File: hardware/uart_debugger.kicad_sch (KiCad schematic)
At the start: 3 parts, among them Q3 JSM2302, U3 CH340E UART Module

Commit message: Added switch footprint, SparkFun_LiPower footprint
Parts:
- U3: now left out of the parts list
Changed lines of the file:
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@@
 		(unit 1)
 		(exclude_from_sim no)
-		(in_bom yes)
+		(in_bom no)
 		(on_board yes)
 		(dnp no)

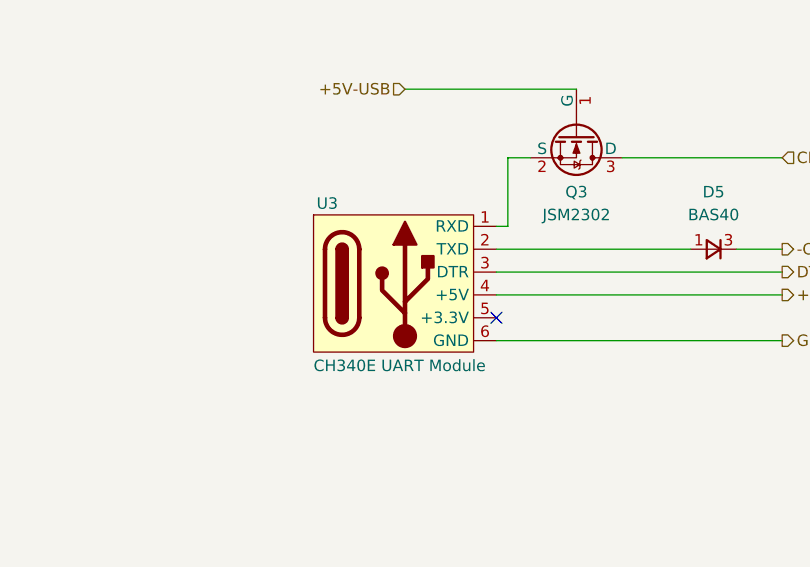
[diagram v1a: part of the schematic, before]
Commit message: Added many footprints and populated part of the property tables
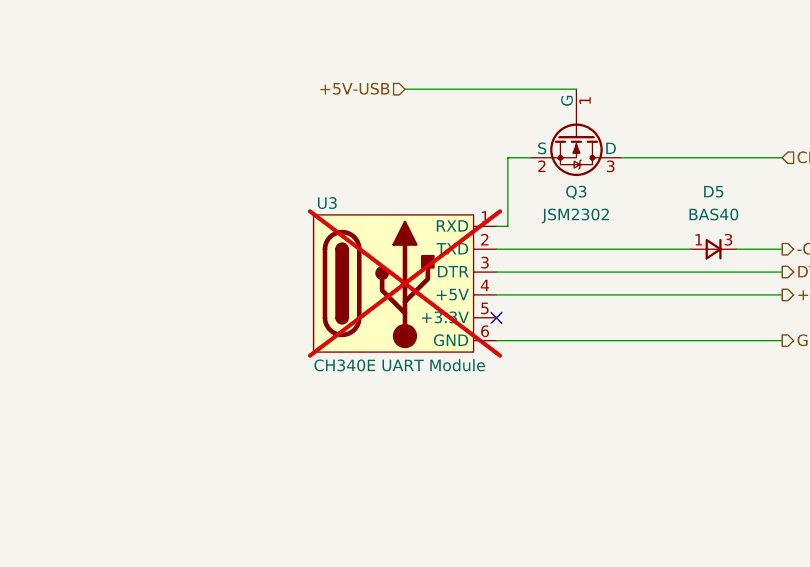
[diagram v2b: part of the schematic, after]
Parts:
- U3: now not fitted
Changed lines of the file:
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@@
 		(in_bom no)
 		(on_board yes)
-		(dnp no)
+		(dnp yes)
 		(property "Reference" "U3"
 			(at 117.094 95.25 0)

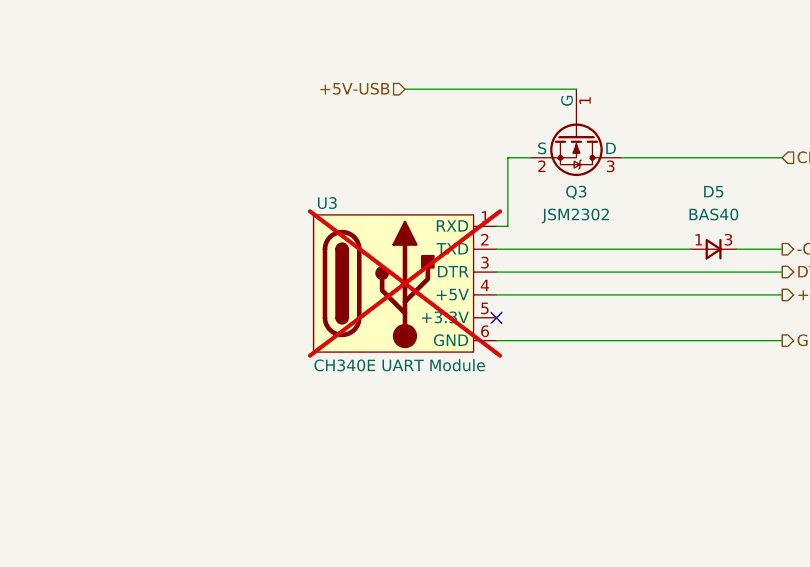
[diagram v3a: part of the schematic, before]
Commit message: Made some small changes on the properties of some components while having last weeks meeting and added the fp-info-cache to the gitignore file
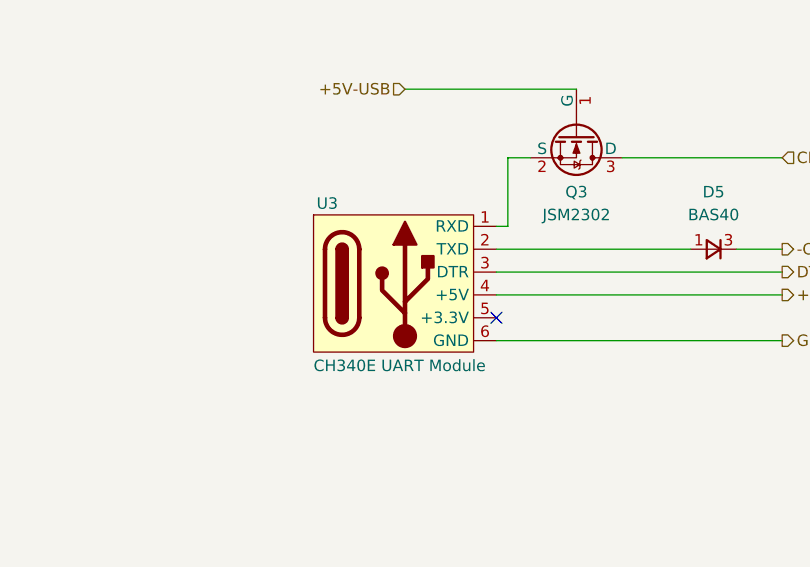
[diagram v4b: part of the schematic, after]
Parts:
- U3: now fitted
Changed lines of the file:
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@@
 		(in_bom no)
 		(on_board yes)
-		(dnp yes)
+		(dnp no)
 		(property "Reference" "U3"
 			(at 117.094 95.25 0)

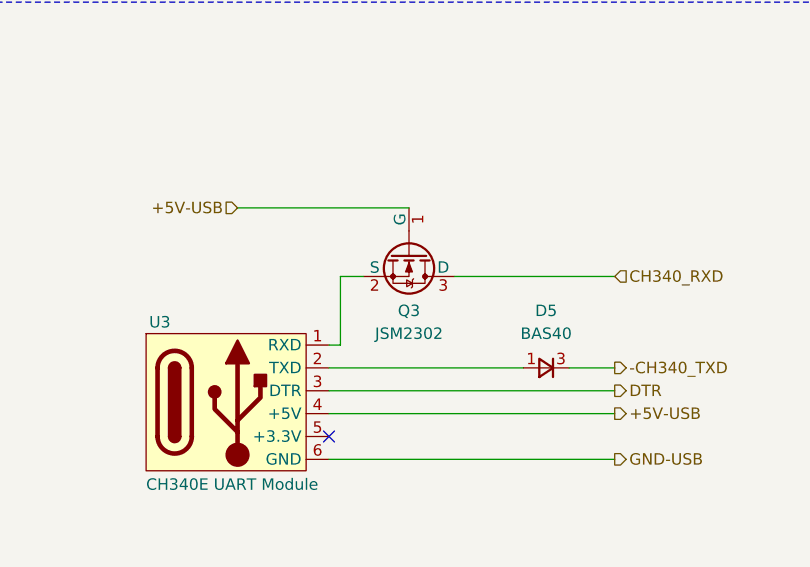
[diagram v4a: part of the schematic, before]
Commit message: Symbols pins vs footprint pins checked
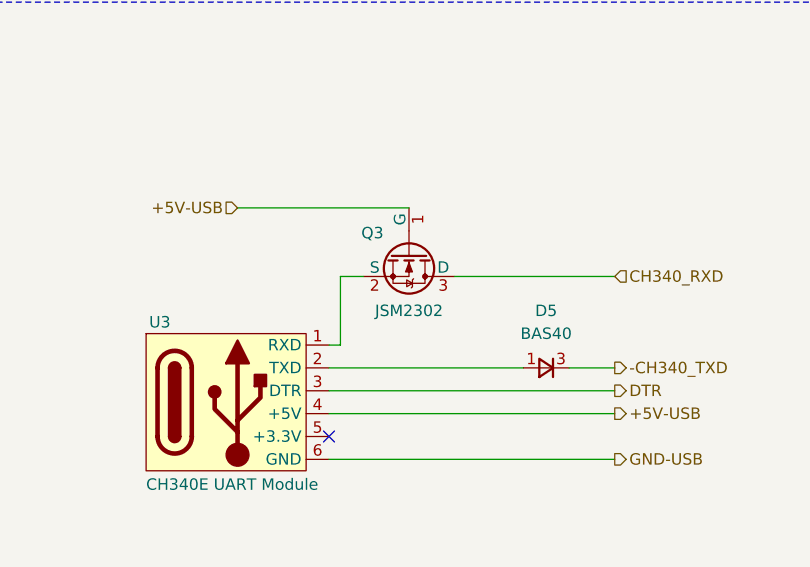
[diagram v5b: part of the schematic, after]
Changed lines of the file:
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@@
 		(dnp no)
 		(property "Reference" "Q3"
-			(at 144.78 93.98 90)
+			(at 140.716 85.344 90)
 			(effects
 				(font
@@
 		)
 		(property "Value" "JSM2302"
-			(at 144.78 96.52 90)
+			(at 144.78 93.98 90)
 			(effects
 				(font

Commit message: Electric Rules Check completed.
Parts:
- removed D5: BAS40, Package_TO_SOT_SMD:SOT-23, symbol Device:D_Small
- removed Q3: JSM2302, Package_TO_SOT_SMD:SOT-23, symbol Simulation_SPICE:NMOS
- added D2: BAS40, Package_TO_SOT_SMD:SOT-23, symbol kitchen_timer-symbols_lib:BAS40_diode
- added Q4: JSM2302, Package_TO_SOT_SMD:SOT-23, symbol kitchen_timer-symbols_lib:JSM2302
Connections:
- net +5V-USB: now also Q4.1 (G)
- net CH340_RXD: now also Q4.3 (D)
- net ­CH340_TXD: now also D2.3 (K)
- net at U3.1 (RXD): now also Q4.2 (S)
- net at U3.2 (TXD): now also D2.1 (A)
- net GND-USB renamed GND
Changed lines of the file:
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@@
 	)
 	(hierarchical_label "+5V-USB"
-		(shape input)
+		(shape output)
 		(at 125.73 82.55 180)
 		(effects
@@
 		)
 	)
-	(hierarchical_label "GND-USB"
+	(hierarchical_label "GND"
 		(shape output)
 		(at 167.64 110.49 0)
@@
 	)
 	(symbol
-		(lib_id "Simulation_SPICE:NMOS")
+		(lib_id "kitchen_timer-symbols_lib:BAS40_diode")
+		(at 160.02 100.33 180)
+		(unit 1)
+		(exclude_from_sim no)
+		(in_bom yes)
+		(on_board yes)
+		(dnp no)
+		(fields_autoplaced yes)
+		(property "Reference" "D2"
+			(at 160.02 93.98 0)
+			(effects
+				(font
+					(size 1.27 1.27)
+				)
+			)
+		)
+		(property "Value" "BAS40"
+			(at 160.02 96.52 0)
+			(effects
+				(font
+					(size 1.27 1.27)
+				)
+			)
+		)
+		(property "Footprint" "Package_TO_SOT_SMD:SOT-23"
+			(at 138.938 100.076 90)
+			(effects
+				(font
+					(size 1.27 1.27)
+				)
+				(hide yes)
+			)
+		)
+		(property "Datasheet" "https://jlcpcb.com/api/file/downloadByFileSystemAccessId/8590224761860497408"
+			(at 142.748 101.092 90)
+			(effects
+				(font
+					(size 1.27 1.27)
+				)
+				(hide yes)
+			)
+		)
+		(property "Description" "40V Independent Type 200mA 1V@40mA SOT-23 Schottky Diodes ROHS"
+			(at 158.75 118.872 0)
+			(effects
+				(font
+					(size 1.27 1.27)
+				)
+				(hide yes)
+			)
+		)
+		(property "Sim.Pins" "1=K 2=A"
+			(at 148.844 110.998 0)
+			(effects
+				(font
+					(size 1.27 1.27)
+				)
+				(hide yes)
+			)
+		)
+		(property "Supplier Link" "https://jlcpcb.com/partdetail/78417-BAS40/C77289"
+			(at 156.21 121.412 0)
+			(effects
+				(font
+					(size 1.27 1.27)
+				)
+				(hide yes)
+			)
+		)
+		(property "Package" "SOT-23"
+			(at 158.496 115.316 0)
+			(effects
+				(font
+					(size 1.27 1.27)
+				)
+				(hide yes)
+			)
+		)
+		(property "Supplier Name" "JLCPCB"
+			(at 160.02 100.33 0)
+			(effects
+				(font
+					(size 1.27 1.27)
+				)
+				(hide yes)
+			)
+		)
+		(property "Manuf. Part #" "BAS40"
+			(at 160.02 100.33 0)
+			(effects
+				(font
+					(size 1.27 1.27)
+				)
+				(hide yes)
+			)
+		)
+		(property "Supplier Unit Price" "$0.0257"
+			(at 160.02 100.33 0)
+			(effects
+				(font
+					(size 1.27 1.27)
+				)
+				(hide yes)
+			)
+		)
+		(property "Part Num" "NA"
+			(at 160.02 100.33 0)
+			(effects
+				(font
+					(size 1.27 1.27)
+				)
+				(hide yes)
+			)
+		)
+		(property "Manuf. Name" "Jiangsu Changjing Electronics Technology Co., Ltd."
+			(at 160.02 100.33 0)
+			(effects
+				(font
+					(size 1.27 1.27)
+				)
+				(hide yes)
+			)
+		)
+		(property "Supplier Part #" " C77289"
+			(at 160.02 100.33 0)
+			(effects
+				(font
+					(size 1.27 1.27)
+				)
+				(hide yes)
+			)
+		)
+		(pin "3"
+		)
+		(pin "1"
+		)
+		(instances
+			(project ""
+				(path "/8963deea-96bc-4401-b671-98fbe9ed9c6a/f7e640d9-c0d9-4c44-8592-f18e152ed7d5"
+					(reference "D2")
+					(unit 1)
+				)
+			)
+		)
+	)
+	(symbol
+		(lib_id "kitchen_timer-symbols_lib:JSM2302")
 		(at 144.78 87.63 270)
 		(unit 1)
@@
 		(on_board yes)
 		(dnp no)
-		(property "Reference" "Q3"
-			(at 140.716 85.344 90)
+		(property "Reference" "Q4"
+			(at 140.208 84.836 90)
 			(effects
 				(font
@@
 		)
 		(property "Value" "JSM2302"
-			(at 144.78 93.98 90)
+			(at 144.78 93.726 90)
 			(effects
 				(font
@@
 			)
 		)
-		(property "Sim.Type" "VDMOS"
+		(property "Sim.Type" ""
 			(at 125.73 87.63 0)
 			(effects
@@
 			)
 		)
-		(property "Sim.Pins" "1=D 2=G 3=S"
+		(property "Sim.Pins" ""
 			(at 129.54 87.63 0)
 			(effects
@@
 			(project ""
 				(path "/8963deea-96bc-4401-b671-98fbe9ed9c6a/f7e640d9-c0d9-4c44-8592-f18e152ed7d5"
-					(reference "Q3")
+					(reference "Q4")
 					(unit 1)
 				)
-			)
-		)
-	)
-	(symbol
-		(lib_name "D_Small_1")
-		(lib_id "Device:D_Small")
-		(at 160.02 100.33 0)
-		(mirror y)
-		(unit 1)
-		(exclude_from_sim no)
-		(in_bom yes)
-		(on_board yes)
-		(dnp no)
-		(property "Reference" "D5"
-			(at 160.02 93.98 0)
-			(effects
-				(font
-					(size 1.27 1.27)
-				)
-			)
-		)
-		(property "Value" "BAS40"
-			(at 160.02 96.52 0)
-			(effects
-				(font
-					(size 1.27 1.27)
-				)
-			)
-		)
-		(property "Footprint" "Package_TO_SOT_SMD:SOT-23"
-			(at 138.938 100.584 90)
-			(effects
-				(font
-					(size 1.27 1.27)
-				)
-				(hide yes)
-			)
-		)
-		(property "Datasheet" "https://jlcpcb.com/api/file/downloadByFileSystemAccessId/8590224761860497408"
-			(at 142.748 99.568 90)
-			(effects
-				(font
-					(size 1.27 1.27)
-				)
-				(hide yes)
-			)
-		)
-		(property "Description" "40V Independent Type 200mA 1V@40mA SOT-23 Schottky Diodes ROHS"
-			(at 158.75 81.788 0)
-			(effects
-				(font
-					(size 1.27 1.27)
-				)
-				(hide yes)
-			)
-		)
-		(property "Sim.Pins" "1=K 2=A"
-			(at 148.844 89.662 0)
-			(effects
-				(font
-					(size 1.27 1.27)
-				)
-				(hide yes)
-			)
-		)
-		(property "Supplier Link" "https://jlcpcb.com/partdetail/78417-BAS40/C77289"
-			(at 156.21 79.248 0)
-			(effects
-				(font
-					(size 1.27 1.27)
-				)
-				(hide yes)
-			)
-		)
-		(property "Package" "SOT-23"
-			(at 158.496 85.344 0)
-			(effects
-				(font
-					(size 1.27 1.27)
-				)
-				(hide yes)
-			)
-		)
-		(property "Supplier Name" "JLCPCB"
-			(at 160.02 100.33 0)
-			(effects
-				(font
-					(size 1.27 1.27)
-				)
-				(hide yes)
-			)
-		)
-		(property "Manuf. Part #" "BAS40"
-			(at 160.02 100.33 0)
-			(effects
-				(font
-					(size 1.27 1.27)
-				)
-				(hide yes)
-			)
-		)
-		(property "Supplier Unit Price" "$0.0257"
-			(at 160.02 100.33 0)
-			(effects
-				(font
-					(size 1.27 1.27)
-				)
-				(hide yes)
-			)
-		)
-		(property "Part Num" "NA"
-			(at 160.02 100.33 0)
-			(effects
-				(font
-					(size 1.27 1.27)
-				)
-				(hide yes)
-			)
-		)
-		(property "Manuf. Name" "Jiangsu Changjing Electronics Technology Co., Ltd."
-			(at 160.02 100.33 0)
-			(effects
-				(font
-					(size 1.27 1.27)
-				)
-				(hide yes)
-			)
-		)
-		(property "Supplier Part #" " C77289"
-			(at 160.02 100.33 0)
-			(effects
-				(font
-					(size 1.27 1.27)
-				)
-				(hide yes)
-			)
-		)
-		(pin "3"
-		)
-		(pin "1"
-		)
-		(instances
-			(project "kitchen_timer-hardware"
-				(path "/8963deea-96bc-4401-b671-98fbe9ed9c6a/f7e640d9-c0d9-4c44-8592-f18e152ed7d5"
-					(reference "D5")
-					(unit 1)
-				)

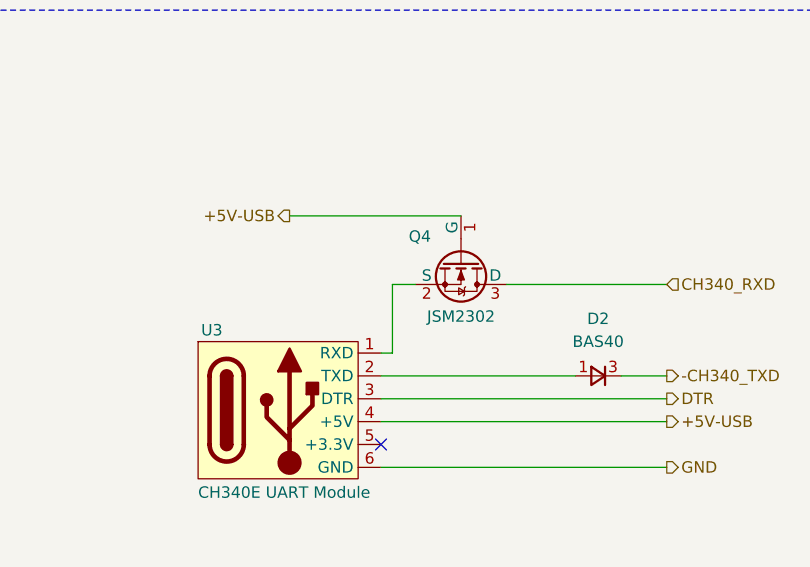
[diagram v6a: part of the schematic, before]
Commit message: Added footprints to mounting holes and selected a part for the test LED.
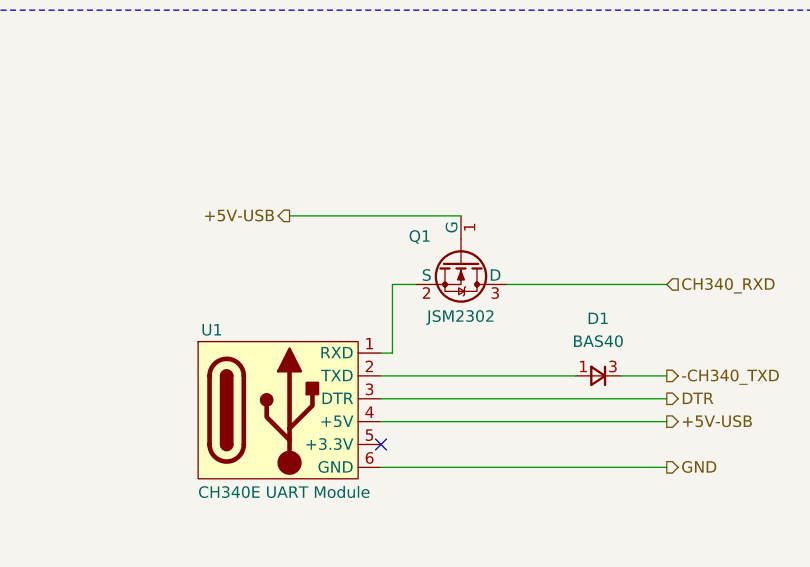
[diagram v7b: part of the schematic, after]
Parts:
- renumbered D2 to D1, Q4 to Q1, U3 to U1
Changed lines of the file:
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@@
 		(on_board yes)
 		(dnp no)
-		(property "Reference" "U3"
+		(property "Reference" "U1"
 			(at 117.094 95.25 0)
 			(effects
@@
 				)
 				(hide yes)
+			)
+		)
+		(property "Manufacturer_Name" ""
+			(at 125.73 104.14 0)
+			(effects
+				(font
+					(size 1.27 1.27)
+				)
+			)
+		)
+		(property "Manufacturer_Part_Number" ""
+			(at 125.73 104.14 0)
+			(effects
+				(font
+					(size 1.27 1.27)
+				)
+			)
+		)
+		(property "Mouser Part Number" ""
+			(at 125.73 104.14 0)
+			(effects
+				(font
+					(size 1.27 1.27)
+				)
+			)
+		)
+		(property "Mouser Price/Stock" ""
+			(at 125.73 104.14 0)
+			(effects
+				(font
+					(size 1.27 1.27)
+				)
 			)
 		)
@@
 			(project "kitchen_timer-hardware"
 				(path "/8963deea-96bc-4401-b671-98fbe9ed9c6a/f7e640d9-c0d9-4c44-8592-f18e152ed7d5"
-					(reference "U3")
+					(reference "U1")
 					(unit 1)
 				)
@@
 		(dnp no)
 		(fields_autoplaced yes)
-		(property "Reference" "D2"
+		(property "Reference" "D1"
 			(at 160.02 93.98 0)
 			(effects
@@
 				)
 				(hide yes)
+			)
+		)
+		(property "Manufacturer_Name" ""
+			(at 160.02 100.33 0)
+			(effects
+				(font
+					(size 1.27 1.27)
+				)
+			)
+		)
+		(property "Manufacturer_Part_Number" ""
+			(at 160.02 100.33 0)
+			(effects
+				(font
+					(size 1.27 1.27)
+				)
+			)
+		)
+		(property "Mouser Part Number" ""
+			(at 160.02 100.33 0)
+			(effects
+				(font
+					(size 1.27 1.27)
+				)
+			)
+		)
+		(property "Mouser Price/Stock" ""
+			(at 160.02 100.33 0)
+			(effects
+				(font
+					(size 1.27 1.27)
+				)
 			)
 		)
@@
 			(project ""
 				(path "/8963deea-96bc-4401-b671-98fbe9ed9c6a/f7e640d9-c0d9-4c44-8592-f18e152ed7d5"
-					(reference "D2")
+					(reference "D1")
 					(unit 1)
 				)
@@
 		(on_board yes)
 		(dnp no)
-		(property "Reference" "Q4"
+		(property "Reference" "Q1"
 			(at 140.208 84.836 90)
 			(effects
@@
 				)
 				(hide yes)
+			)
+		)
+		(property "Manufacturer_Name" ""
+			(at 144.78 87.63 0)
+			(effects
+				(font
+					(size 1.27 1.27)
+				)
+			)
+		)
+		(property "Manufacturer_Part_Number" ""
+			(at 144.78 87.63 0)
+			(effects
+				(font
+					(size 1.27 1.27)
+				)
+			)
+		)
+		(property "Mouser Part Number" ""
+			(at 144.78 87.63 0)
+			(effects
+				(font
+					(size 1.27 1.27)
+				)
+			)
+		)
+		(property "Mouser Price/Stock" ""
+			(at 144.78 87.63 0)
+			(effects
+				(font
+					(size 1.27 1.27)
+				)
 			)
 		)
@@
 			(project ""
 				(path "/8963deea-96bc-4401-b671-98fbe9ed9c6a/f7e640d9-c0d9-4c44-8592-f18e152ed7d5"
-					(reference "Q4")
+					(reference "Q1")
 					(unit 1)
 				)
